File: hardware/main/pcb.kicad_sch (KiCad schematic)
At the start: 27 parts, among them J3 Conn_01x03_Socket, Q1 BC547, Q2 BC547, Q3 BC547

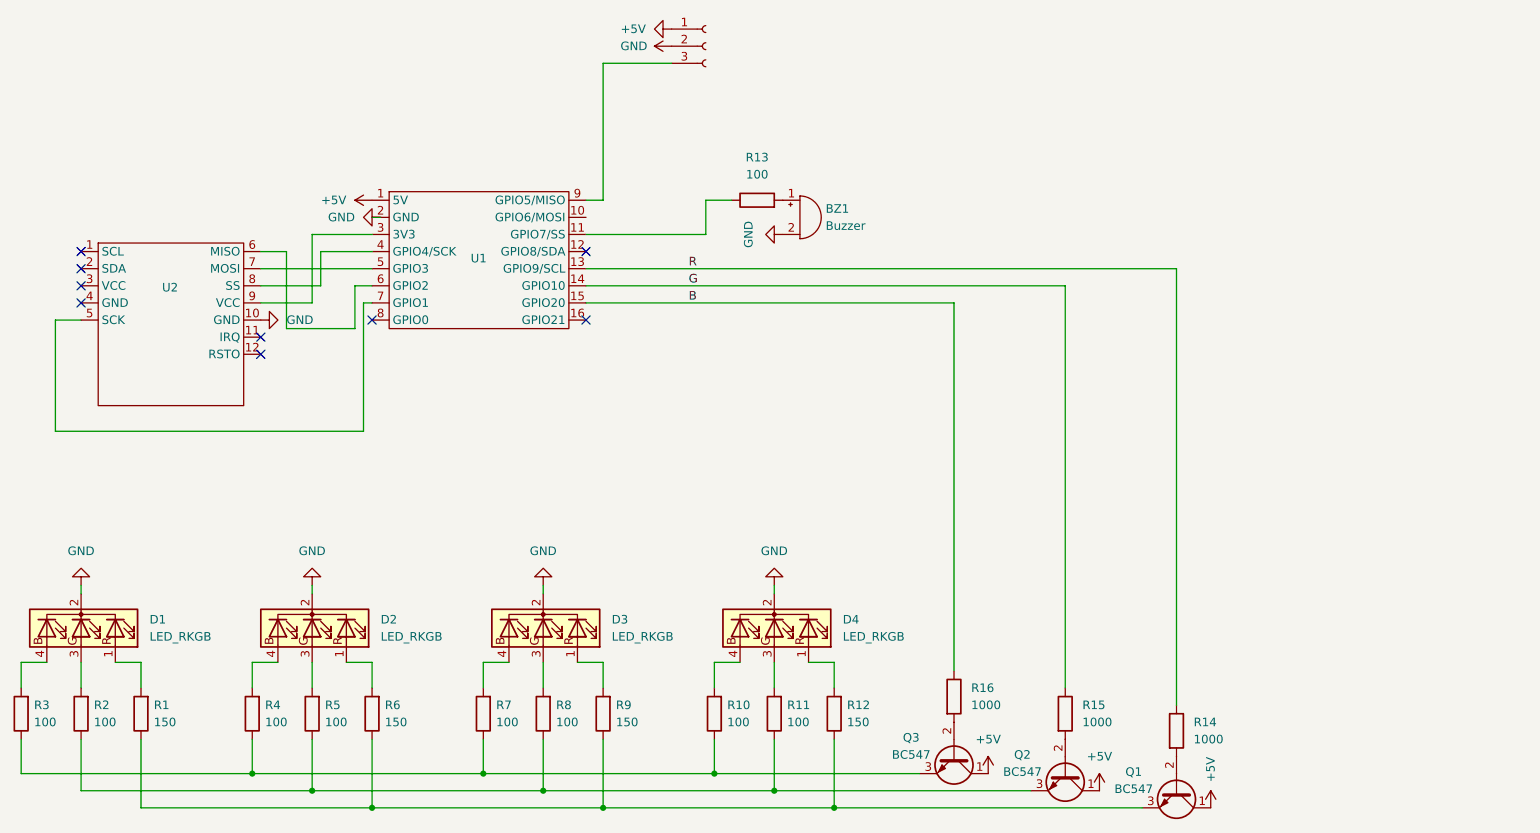
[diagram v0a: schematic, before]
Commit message: Migrate PCB to addressable LEDs, 42x42 mm single-layer board
- Resize board to 42x42 mm with chamfered corners, 1.6 mm thickness
- Move LEDs and JST connector to fit; add GND pointer to LED footprints
- Replace pin socket with 2.54 mm JST footprint with built-in pin labels
- Re-route traces on the back copper layer only
- Move all text to the solder-side silkscreen, drop PN532 silkscreen
- Move libraries to hardware/libs and remove unused footprints/models

Co-Authored-By: Claude Sonnet 5.5 <noreply@anthropic.com>
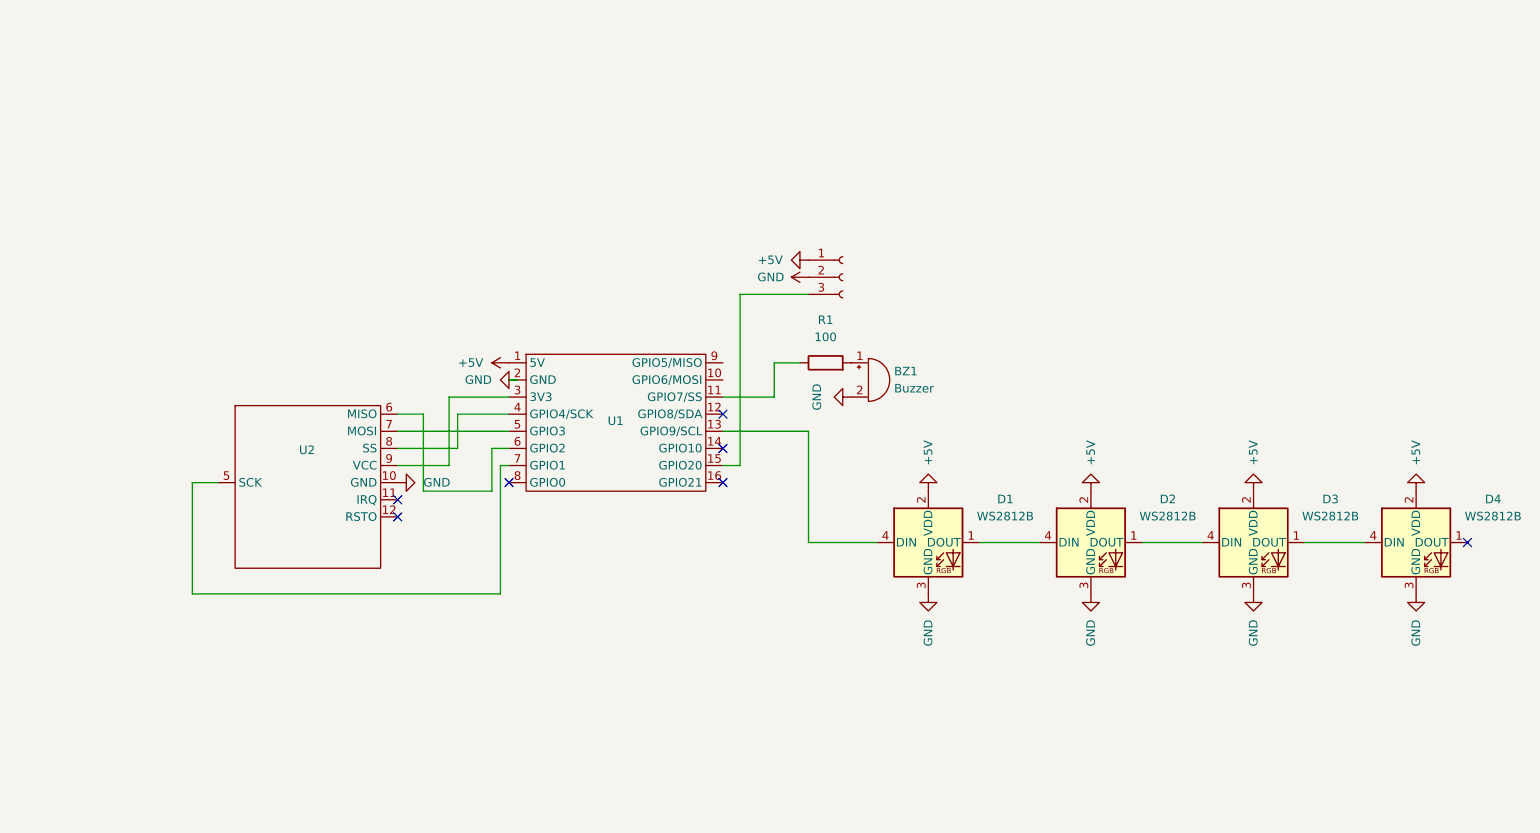
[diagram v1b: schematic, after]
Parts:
- removed D1, D2, D3, D4: LED_RKGB, LED_THT:LED_D5.0mm-4_RGB_Wide_Pins_CNC_read, symbol Device:LED_RKGB
- removed Q1, Q2, Q3: BC547, Package_TO_SOT_THT:TO-92_Inline, symbol Transistor_BJT:BC547
- removed R1, R12, R6, R9: 150, Resistor_THT:CNC_Ready_R_Axial_DIN0204_L3.6mm_D1.6mm_P7.62mm_Horizontal, symbol Device:R
- removed R10, R11, R2, R3, R4, R5, R7, R8: 100, Resistor_THT:CNC_Ready_R_Axial_DIN0204_L3.6mm_D1.6mm_P7.62mm_Horizontal, symbol Device:R
- removed R14, R15, R16: 1000, Resistor_THT:CNC_Ready_R_Axial_DIN0204_L3.6mm_D1.6mm_P7.62mm_Horizontal, symbol Device:R
- added D1, D2, D3, D4: WS2812B, prismo:LED_D5.0mm-2812-D-diagonal, symbol prismo:WS2812-D
- BZ1: footprint Buzzer_Beeper:MagneticBuzzer_ProSignal_ABI-010-RC -> prismo:MagneticBuzzer_ProSignal_ABI-010-RC; symbol Device:Buzzer -> prismo:Buzzer
- J3: footprint Connector_PinSocket_2.54mm:PinSocket_1x03_P2.54mm_Vertical_with_holes -> prismo:JST_1x03_P2.54mm_Vertical; symbol Connector:Conn_01x03_Socket -> prismo:Conn_01x03_Socket
- R1: renamed from R13; footprint Resistor_THT:CNC_Ready_R_Axial_DIN0204_L3.6mm_D1.6mm_P7.62mm_Horizontal -> prismo:R_Axial_DIN0204_L3.6mm_D1.6mm_P7.62mm_Horizontal; symbol Device:R -> prismo:R
- U1: footprint esp_32_c3_supper_mini:esp_32_c3_supper_mini -> prismo:esp_32_c3_supper_mini; symbol esp_c3_32_supper_mini:esp_32_c3_supper_mini -> prismo:esp_32_c3_supper_mini
- U2: footprint esp_32_c3_supper_mini:PN532 NFC RFID simple (one row) -> prismo:PN532 NFC RFID simple (one row); symbol esp_c3_32_supper_mini:PN532_NFC_RFID_module_V3 -> prismo:PN532_NFC_RFID_module_V3
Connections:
- net B is gone; now on an unnamed net: U1.15 (GPIO20)
- net +5V: now also D1.2 (VDD), D2.2 (VDD), D3.2 (VDD), D4.2 (VDD)
- net GND: now also D1.3 (GND), D2.3 (GND), D3.3 (GND), D4.3 (GND)
- net at J3.3 (Pin_3): no longer U1.9 (GPIO5/MISO)
- net G: no longer names the net of U1.14 (GPIO10)
- net R: no longer names the net of U1.13 (GPIO9/SCL)
- net R: now also D1.4 (DIN)
- new net: D3.1 (DOUT), D4.4 (DIN)
- new net: D2.1 (DOUT), D3.4 (DIN)
- new net: D1.1 (DOUT), D2.4 (DIN)
- no-connect marks 9 -> 7
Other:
- moved on the sheet: BZ1, R1, U1

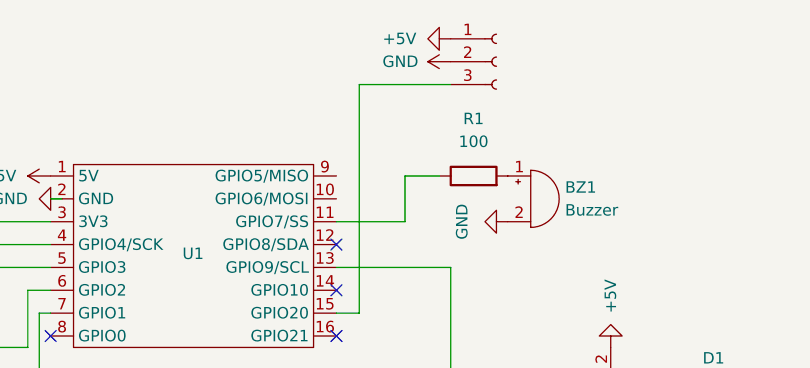
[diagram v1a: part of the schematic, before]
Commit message: Add dcdc board schematic with button input; add SIG isolation diode on main
Co-Authored-By: Claude Sonnet 5.5 <noreply@anthropic.com>
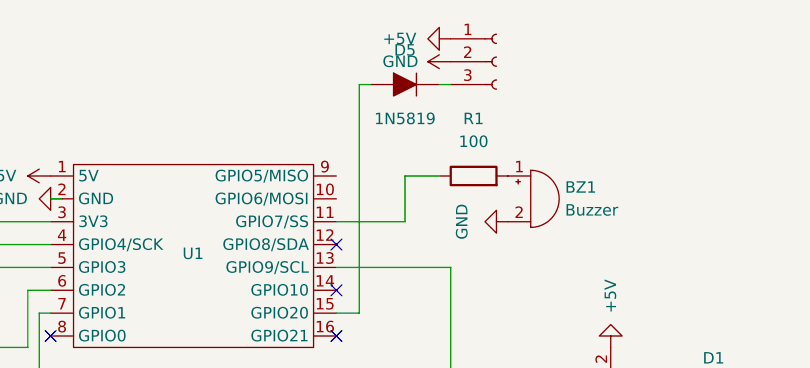
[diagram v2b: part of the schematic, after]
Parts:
- added D5: 1N5819, Diode_THT:D_DO-41_SOD81_P10.16mm_Horizontal, symbol prismo:D_Schottky
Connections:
- net at U1.15 (GPIO20): now also D5.2 (A); no longer J3.3 (Pin_3)
- new net: D5.1 (K), J3.3 (Pin_3)
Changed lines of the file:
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@@
 	(wire
 		(pts
-			(xy 128.27 83.82) (xy 138.43 83.82)
+			(xy 128.27 83.82) (xy 129.54 83.82)
 		)
 		(stroke
@@
 		)
 	)
+	(wire
+		(pts
+			(xy 137.16 83.82) (xy 138.43 83.82)
+		)
+		(stroke
+			(width 0)
+			(type default)
+		)
+	)
+	(symbol
+		(lib_id "prismo:D_Schottky")
+		(at 133.35 83.82 270)
+		(unit 1)
+		(body_style 1)
+		(exclude_from_sim no)
+		(in_bom yes)
+		(on_board yes)
+		(in_pos_files yes)
+		(dnp no)
+		(property "Reference" "D5"
+			(at 133.35 80.01 90)
+			(show_name no)
+			(do_not_autoplace no)
+			(effects
+				(font
+					(size 1.27 1.27)
+				)
+			)
+		)
+		(property "Value" "1N5819"
+			(at 133.35 87.63 90)
+			(show_name no)
+			(do_not_autoplace no)
+			(effects
+				(font
+					(size 1.27 1.27)
+				)
+			)
+		)
+		(property "Footprint" "Diode_THT:D_DO-41_SOD81_P10.16mm_Horizontal"
+			(at 133.35 83.82 0)
+			(hide yes)
+			(show_name no)
+			(do_not_autoplace no)
+			(effects
+				(font
+					(size 1.27 1.27)
+				)
+			)
+		)
+		(pin "1"
+		)
+		(pin "2"
+		)
+		(instances
+			(project "pcb"
+				(path "/e0f69ff1-e3b8-4d01-8d2a-72fcb9b35158"
+					(reference "D5")
+					(unit 1)
+				)
+			)
+		)
+	)
